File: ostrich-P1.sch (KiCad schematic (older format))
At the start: 67 parts

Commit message: About to delete ESP
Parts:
- added 1K? (x2): R, symbol R
- added C?: 100nF, symbol C
- added D? (x4): LED, symbol LED
- added J?: Fil_runout, symbol Conn_01x02
- added J?: Effector, symbol Conn_02x07_Counter_Clockwise
- added J?: Laser, symbol Conn_01x03
- added Q? (x2): S8050, TO_SOT_Packages_THT:TO-92_Molded_Narrow, symbol S8050
- added Q? (x2): IRLZ44N, symbol Q_NMOS_DGS
- added Q?: 2N7002, symbol Q_NMOS_DGS
- added R? (x4): 1K, symbol R
- added R? (x5): 10K, symbol R
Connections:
- net labels added: +5V, EndP, Fan1C, Fan1P, Fan2C, Fan2P, Fil_runout, LasA, LasC, LasP, MISO33, MOSI33, MarlinRXD, MarlinTXD, Probe, SCLK33, Servo, T1, T2
- wire segments 140 -> 228
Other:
- moved on the sheet: R?

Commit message: deleted ESP
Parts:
- removed C?: 10uF, symbol C
- removed C?: 100nF, symbol C
- removed Q?: 2N7002, symbol Q_NMOS_DGS
- removed R?: 1R, symbol R
- removed R? (x5): 10K, symbol R
- removed U?: LM1117-3.3, symbol LM1117-3.3
- removed U?: ESP-12F, symbol ESP-12F
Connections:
- net labels removed: +3.3V, MISO33, MOSI33, MarlinRXD, MarlinTXD, SCLK33
- wire segments 228 -> 189

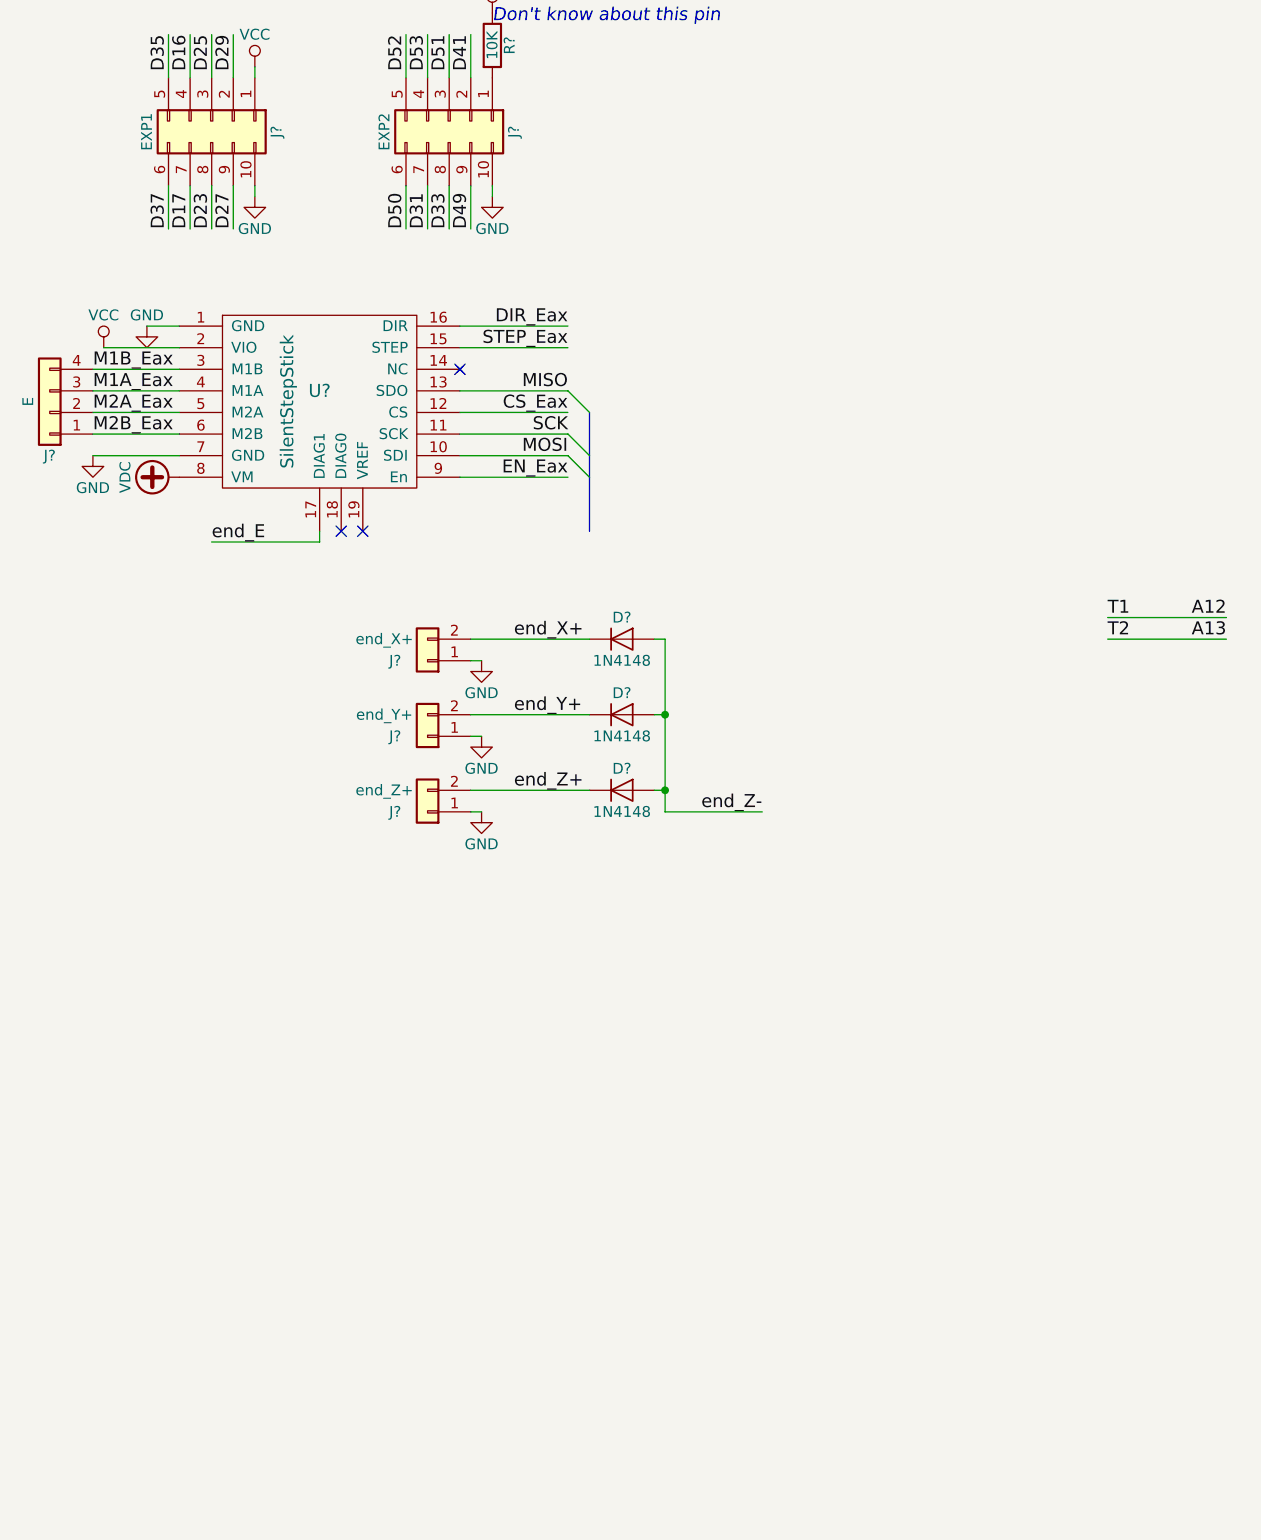
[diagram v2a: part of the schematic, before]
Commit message: added steppers
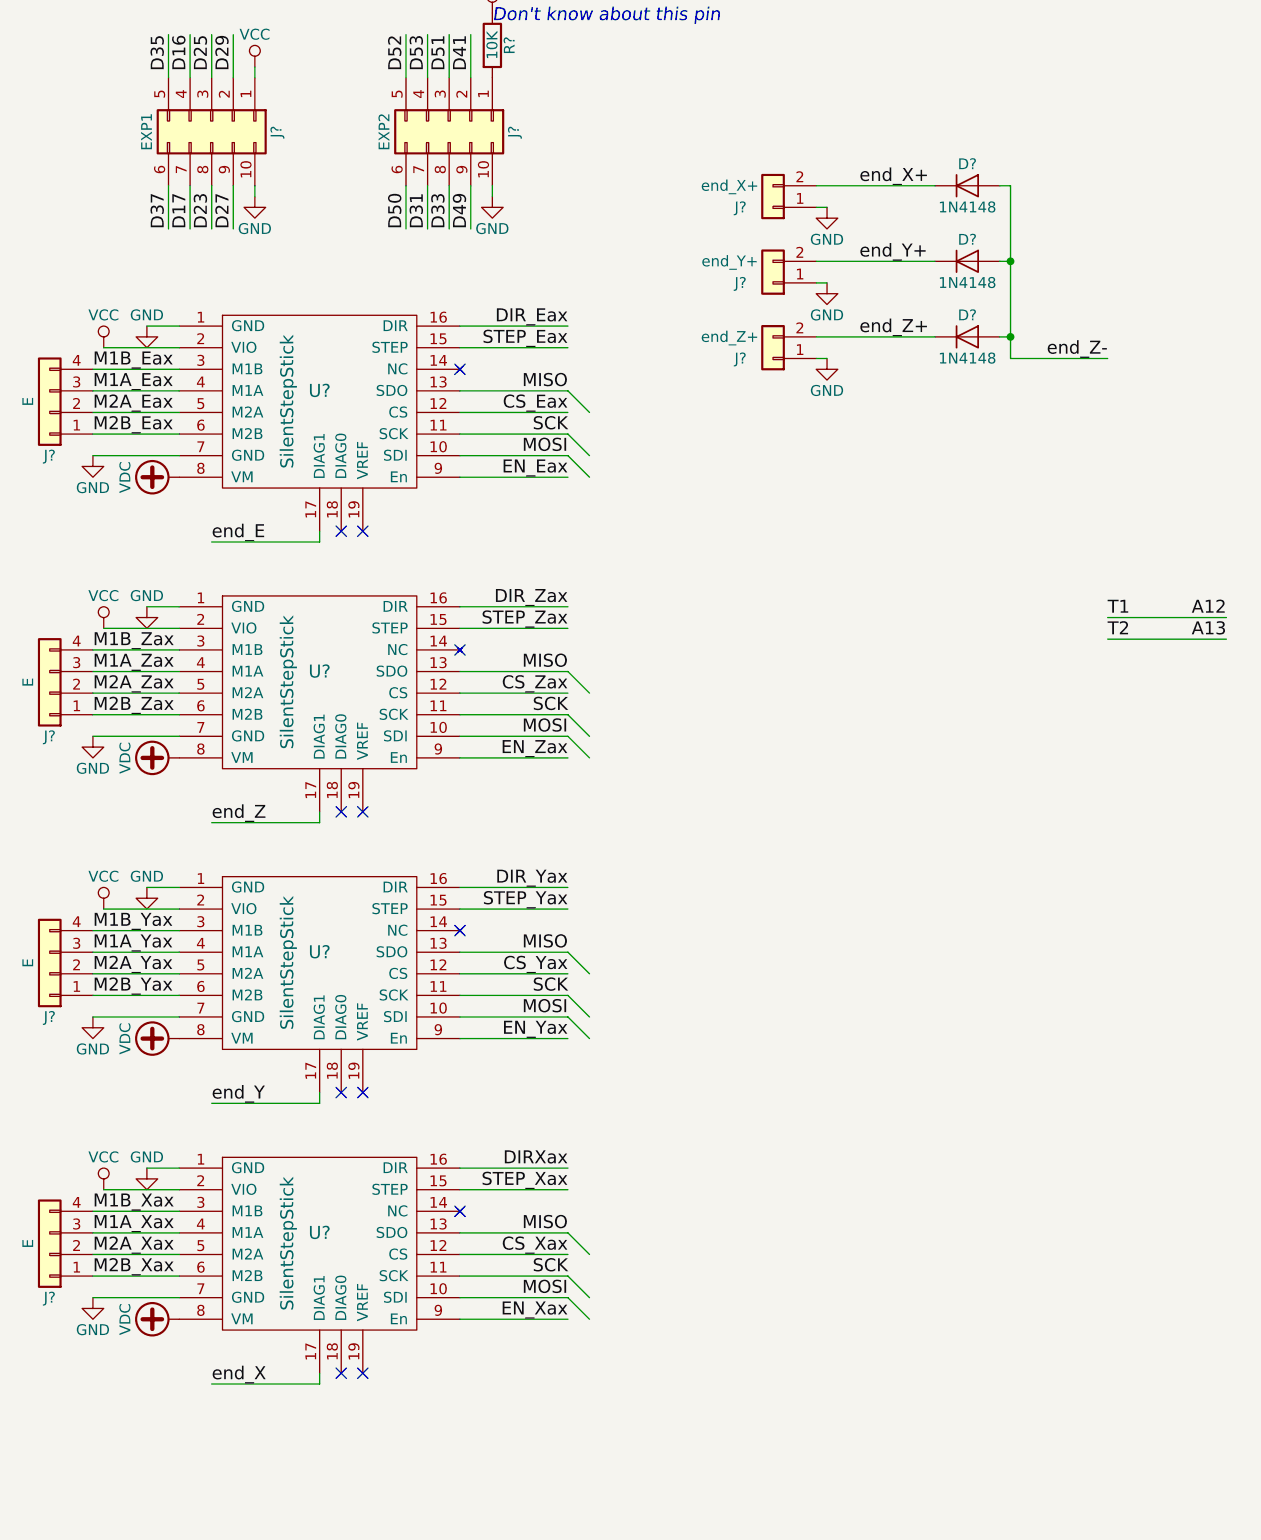
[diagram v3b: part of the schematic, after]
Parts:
- added J? (x3): E, symbol Conn_01x04
- added U? (x3): SilentStepStick, symbol SilentStepStick
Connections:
- net GND: now also U?.1 (GND), U?.1 (GND), U?.1 (GND), U?.7 (GND), U?.7 (GND), U?.7 (GND)
- net MISO: now also U?.13 (SDO), U?.13 (SDO), U?.13 (SDO)
- net MOSI: now also U?.10 (SDI), U?.10 (SDI), U?.10 (SDI)
- net SCK: now also U?.11 (SCK), U?.11 (SCK), U?.11 (SCK)
- net VCC: now also U?.2 (VIO), U?.2 (VIO), U?.2 (VIO)
- net VDC: now also U?.8 (VM), U?.8 (VM), U?.8 (VM)
- new net CS_Xax: U?.12 (CS)
- new net CS_Yax: U?.12 (CS)
- new net CS_Zax: U?.12 (CS)
- new net DIRXax: U?.16 (DIR)
- new net DIR_Yax: U?.16 (DIR)
- new net DIR_Zax: U?.16 (DIR)
- new net EN_Xax: U?.9 (En)
- new net EN_Yax: U?.9 (En)
- new net EN_Zax: U?.9 (En)
- new net M1A_Xax: J?.3 (Pin_3), U?.4 (M1A)
- new net M1A_Yax: J?.3 (Pin_3), U?.4 (M1A)
- new net M1A_Zax: J?.3 (Pin_3), U?.4 (M1A)
- new net M1B_Xax: J?.4 (Pin_4), U?.3 (M1B)
- new net M1B_Yax: J?.4 (Pin_4), U?.3 (M1B)
- new net M1B_Zax: J?.4 (Pin_4), U?.3 (M1B)
- new net M2A_Xax: J?.2 (Pin_2), U?.5 (M2A)
- new net M2A_Yax: J?.2 (Pin_2), U?.5 (M2A)
- new net M2A_Zax: J?.2 (Pin_2), U?.5 (M2A)
- new net M2B_Xax: J?.1 (Pin_1), U?.6 (M2B)
- new net M2B_Yax: J?.1 (Pin_1), U?.6 (M2B)
- new net M2B_Zax: J?.1 (Pin_1), U?.6 (M2B)
- new net STEP_Xax: U?.15 (STEP)
- new net STEP_Yax: U?.15 (STEP)
- new net STEP_Zax: U?.15 (STEP)
- new net end_X: U?.17 (DIAG1)
- new net end_Y: U?.17 (DIAG1)
- new net end_Z: U?.17 (DIAG1)
- no-connect marks 3 -> 12
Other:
- moved on the sheet: D?, J?

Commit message: Added relay
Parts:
- added 1K: R, symbol R
- added D?: 1N4148, symbol D
- added D?: LED, symbol LED
- added J?: PSU, symbol Conn_01x07
- added J?: Live, symbol Conn_01x01
- added J?: Earth, symbol Conn_01x01
- added J?: Neutral, symbol Conn_01x01
- added J?: On button, symbol Conn_01x02
- added K?: SRD-05VDC-SL-C, Relays_THT:Relay_SPDT_SANYOU_SRD_Series_Form_C, symbol SANYOU_SRD_Form_C
- added Q?: S8050, TO_SOT_Packages_THT:TO-92_Molded_Narrow, symbol S8050
- added R? (x2): 1K, symbol R
- added SW?: SW_Push, symbol SW_Push
- R?: renamed from 1K; value R -> 1K
- R? (x2): renamed from 1K?; value R -> 1K
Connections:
- net Earth_Protective: now also J?.1 (Pin_1)
- net GND: now also D?.1 (K), J?.4 (Pin_4), Q?.1 (E), SW?.1
- net NEUT: now also J?.1 (Pin_1), J?.2 (Pin_2)
- net VAC: now also J?.1 (Pin_1), J?.1 (Pin_1), K?.4
- net VCC: now also 1K.2, D?.1 (K), K?.5, R?.1
- net VDC: now also J?.6 (Pin_6)
- new net: J?.1 (Pin_1), J?.2 (Pin_2), K?.1
- new net: D?.2 (A), K?.2, Q?.3 (C)
- new net: Q?.2 (B), R?.1
- new net: D?.2 (A), R?.2
- new net OffC: 1K.1, R?.2, SW?.2
- no-connect marks 12 -> 14
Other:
- moved on the sheet: D?, J?, Q?, R?

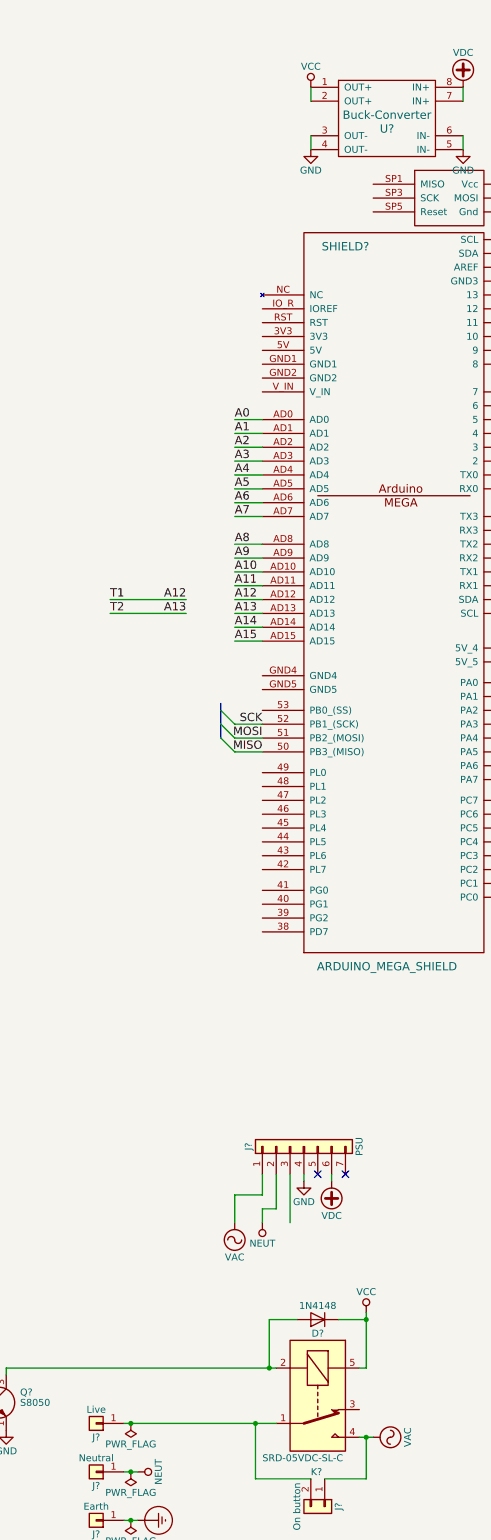
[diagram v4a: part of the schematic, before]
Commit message: fuses added
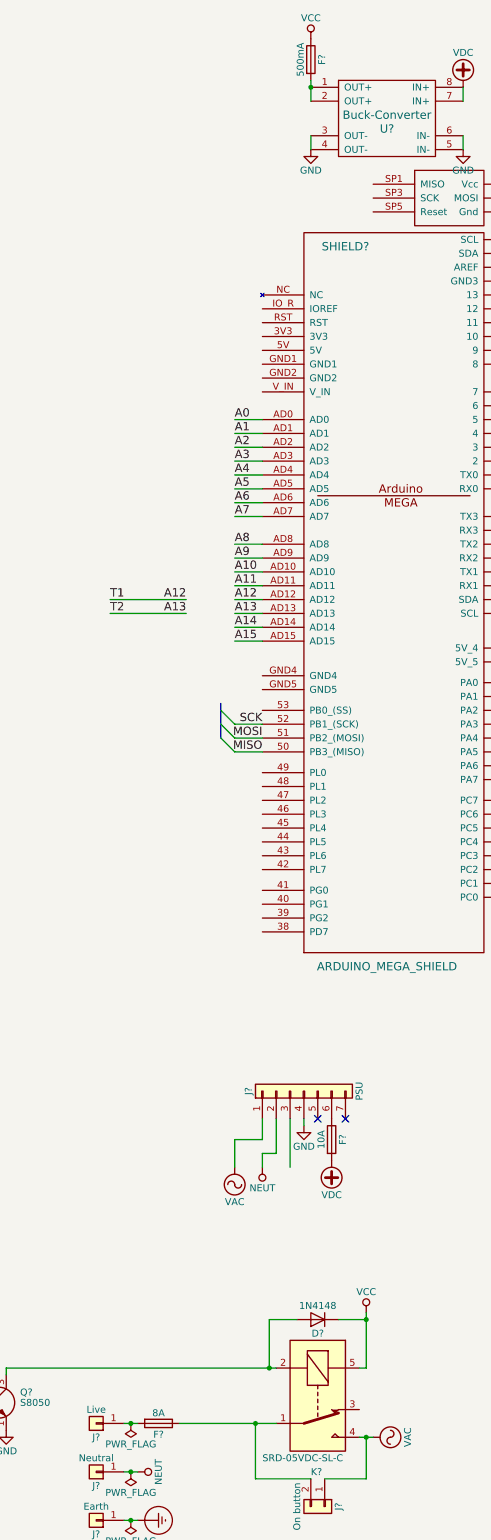
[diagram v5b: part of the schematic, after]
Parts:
- added F?: 500mA, symbol Fuse
- added F?: 10A, symbol Fuse
- added F?: 8A, symbol Fuse
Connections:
- net VCC: now also F?.1; no longer U?.1 (OUT+), U?.2 (OUT+)
- net VDC: now also F?.2; no longer J?.6 (Pin_6)
- net at J?.2 (Pin_2), K?.1: now also F?.1; no longer J?.1 (Pin_1)
- new net: F?.2, U?.1 (OUT+), U?.2 (OUT+)
- new net: F?.1, J?.6 (Pin_6)
- new net: F?.2, J?.1 (Pin_1)
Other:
- moved on the sheet: J?
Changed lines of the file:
@@
 L VCC #PWR031
 U 1 1 5AFC334E
-P 5850 -200
-F 0 "#PWR031" H 5850 -350 50  0001 C CNN
-F 1 "VCC" H 5850 -50 50  0000 C CNN
-F 2 "" H 5850 -200 50  0001 C CNN
-F 3 "" H 5850 -200 50  0001 C CNN
-	1    5850 -200
+P 5850 -550
+F 0 "#PWR031" H 5850 -700 50  0001 C CNN
+F 1 "VCC" H 5850 -400 50  0000 C CNN
+F 2 "" H 5850 -550 50  0001 C CNN
+F 3 "" H 5850 -550 50  0001 C CNN
+	1    5850 -550
 	1    0    0    -1
 $EndComp
@@
 	6950 -100 6950 -200
 Wire Wire Line
-	5850 -200 5850 -100
+	5850 -250 5850 -100
 Wire Wire Line
 	5850 150  5850 250
@@
 L Conn_01x07 J?
 U 1 1 5AFF1AEC
-P 5800 7450
-F 0 "J?" H 5800 7850 50  0000 C CNN
-F 1 "PSU" H 5800 7050 50  0000 C CNN
-F 2 "" H 5800 7450 50  0001 C CNN
-F 3 "" H 5800 7450 50  0001 C CNN
-	1    5800 7450
+P 5800 7050
+F 0 "J?" H 5800 7450 50  0000 C CNN
+F 1 "PSU" H 5800 6650 50  0000 C CNN
+F 2 "" H 5800 7050 50  0001 C CNN
+F 3 "" H 5800 7050 50  0001 C CNN
+	1    5800 7050
 	0    -1   -1   0
 $EndComp
@@
 L NEUT #PWR073
 U 1 1 5AFF3D4F
-P 5500 8000
-F 0 "#PWR073" H 5500 7850 50  0001 C CNN
-F 1 "NEUT" H 5500 8150 50  0000 C CNN
-F 2 "" H 5500 8000 50  0001 C CNN
-F 3 "" H 5500 8000 50  0001 C CNN
-	1    5500 8000
+P 5500 7600
+F 0 "#PWR073" H 5500 7450 50  0001 C CNN
+F 1 "NEUT" H 5500 7750 50  0000 C CNN
+F 2 "" H 5500 7600 50  0001 C CNN
+F 3 "" H 5500 7600 50  0001 C CNN
+	1    5500 7600
 	-1   0    0    1
 $EndComp
@@
 L GND #PWR075
 U 1 1 5AFF4DFB
-P 5800 7700
-F 0 "#PWR075" H 5800 7450 50  0001 C CNN
-F 1 "GND" H 5800 7550 50  0000 C CNN
-F 2 "" H 5800 7700 50  0001 C CNN
-F 3 "" H 5800 7700 50  0001 C CNN
-	1    5800 7700
-	1    0    0    -1
-$EndComp
-$Comp
-L VDC #PWR076
-U 1 1 5AFF53A1
-P 6000 7700
-F 0 "#PWR076" H 6000 7600 50  0001 C CNN
-F 1 "VDC" H 6000 7950 50  0000 C CNN
-F 2 "" H 6000 7700 50  0001 C CNN
-F 3 "" H 6000 7700 50  0001 C CNN
-	1    6000 7700
-	-1   0    0    1
-$EndComp
-Wire Wire Line
-	5700 7650 5700 8000
-Wire Wire Line
-	5600 7650 5600 7900
-Wire Wire Line
-	5600 7900 5500 7900
-Wire Wire Line
-	5500 7900 5500 8000
-Wire Wire Line
-	5500 7650 5500 7800
-Wire Wire Line
-	5500 7800 5300 7800
-Wire Wire Line
-	5300 7800 5300 8000
-Wire Wire Line
-	5800 7650 5800 7700
-Wire Wire Line
-	6000 7700 6000 7650
-NoConn ~ 5900 7650
-NoConn ~ 6100 7650
+P 5800 7300
+F 0 "#PWR075" H 5800 7050 50  0001 C CNN
+F 1 "GND" H 5800 7150 50  0000 C CNN
+F 2 "" H 5800 7300 50  0001 C CNN
+F 3 "" H 5800 7300 50  0001 C CNN
+	1    5800 7300
+	1    0    0    -1
+$EndComp
+Wire Wire Line
+	5700 7250 5700 7600
+Wire Wire Line
+	5600 7250 5600 7500
+Wire Wire Line
+	5600 7500 5500 7500
+Wire Wire Line
+	5500 7500 5500 7600
+Wire Wire Line
+	5500 7250 5500 7400
+Wire Wire Line
+	5500 7400 5300 7400
+Wire Wire Line
+	5300 7400 5300 7600
+Wire Wire Line
+	5800 7250 5800 7300
+NoConn ~ 5900 7250
+NoConn ~ 6100 7250
 $Comp
 L Conn_01x01 J?
@@
 L VAC #PWR077
 U 1 1 5AFF9686
-P 5300 8000
-F 0 "#PWR077" H 5300 7900 50  0001 C CNN
-F 1 "VAC" H 5300 8250 50  0000 C CNN
-F 2 "" H 5300 8000 50  0001 C CNN
-F 3 "" H 5300 8000 50  0001 C CNN
-	1    5300 8000
+P 5300 7600
+F 0 "#PWR077" H 5300 7500 50  0001 C CNN
+F 1 "VAC" H 5300 7850 50  0000 C CNN
+F 2 "" H 5300 7600 50  0001 C CNN
+F 3 "" H 5300 7600 50  0001 C CNN
+	1    5300 7600
 	-1   0    0    1
 $EndComp
@@
 Wire Wire Line
 	4500 9800 4600 9800
-Wire Wire Line
-	4500 9450 5600 9450
 $Comp
 L PWR_FLAG #FLG?
@@
 	1    0    0    -1
 $EndComp
+$Comp
+L Fuse F?
+U 1 1 5B0086B8
+P 5850 -400
+F 0 "F?" V 5930 -400 50  0000 C CNN
+F 1 "500mA" V 5775 -400 50  0000 C CNN
+F 2 "" V 5780 -400 50  0001 C CNN
+F 3 "" H 5850 -400 50  0001 C CNN
+	1    5850 -400
+	1    0    0    -1
+$EndComp
+Connection ~ 5850 -200
+$Comp
+L Fuse F?
+U 1 1 5B00D2B4
+P 6000 7400
+F 0 "F?" V 6080 7400 50  0000 C CNN
+F 1 "10A" V 5925 7400 50  0000 C CNN
+F 2 "" V 5930 7400 50  0001 C CNN
+F 3 "" H 6000 7400 50  0001 C CNN
+	1    6000 7400
+	1    0    0    -1
+$EndComp
+$Comp
+L VDC #PWR?
+U 1 1 5B00E575
+P 6000 7550
+F 0 "#PWR?" H 6000 7450 50  0001 C CNN
+F 1 "VDC" H 6000 7800 50  0000 C CNN
+F 2 "" H 6000 7550 50  0001 C CNN
+F 3 "" H 6000 7550 50  0001 C CNN
+	1    6000 7550
+	-1   0    0    1
+$EndComp
+$Comp
+L Fuse F?
+U 1 1 5B00F526
+P 4750 9450
+F 0 "F?" V 4830 9450 50  0000 C CNN
+F 1 "8A" V 4675 9450 50  0000 C CNN
+F 2 "" V 4680 9450 50  0001 C CNN
+F 3 "" H 4750 9450 50  0001 C CNN
+	1    4750 9450
+	0    1    1    0
+$EndComp
+Wire Wire Line
+	4500 9450 4600 9450
+Wire Wire Line
+	4900 9450 5600 9450
 $EndSCHEMATC
